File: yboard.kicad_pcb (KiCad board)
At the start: 2 copper layers, 192.5 x 63.5 mm, 27 parts, among them J1 JOYPORT_OUT, J2 CONN_D, J3 CONN_F, SW1 FIRE_BTN, SW2 B_BTN, SW3 A_BTN, SW4 RIGHT_BTN, SW5 LEFT_BTN, SW6 DOWN_BTN, SW7 UP_BTN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

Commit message: YBoard rename within the designs
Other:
- board text added: "YBoard DirBoard v 1.0"
- board text added: "YBoard FireBoard"
- board text removed: "JoyBoard DirBoard v 1.0"
- board text removed: "JoyBoard FireBoard"
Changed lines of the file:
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@@
 	(paper "A4")
 	(title_block
-		(title "Amiga JoyBoard")
+		(title "YBoard")
 		(date "2024-07-12")
-		(rev "1.0")
+		(rev "1.1")
 		(company "Kot_Behemot")
 	)
@@
 		)
 	)
-	(gr_text "JoyBoard FireBoard"
-		(at 190.5 69.85 0)
+	(gr_text "YBoard FireBoard"
+		(at 190.5 70.104 0)
 		(layer "B.Cu" knockout)
 		(effects
@@
 		)
 	)
-	(gr_text "JoyBoard DirBoard\nv 1.0"
+	(gr_text "YBoard DirBoard\nv 1.0"
 		(at 128.524 88.646 0)
 		(layer "B.Cu" knockout)
@@
 	)
 	(gr_text "v 1.0"
-		(at 190.5 73.152 0)
+		(at 190.5762 72.8218 0)
 		(layer "B.Cu" knockout)
 		(effects

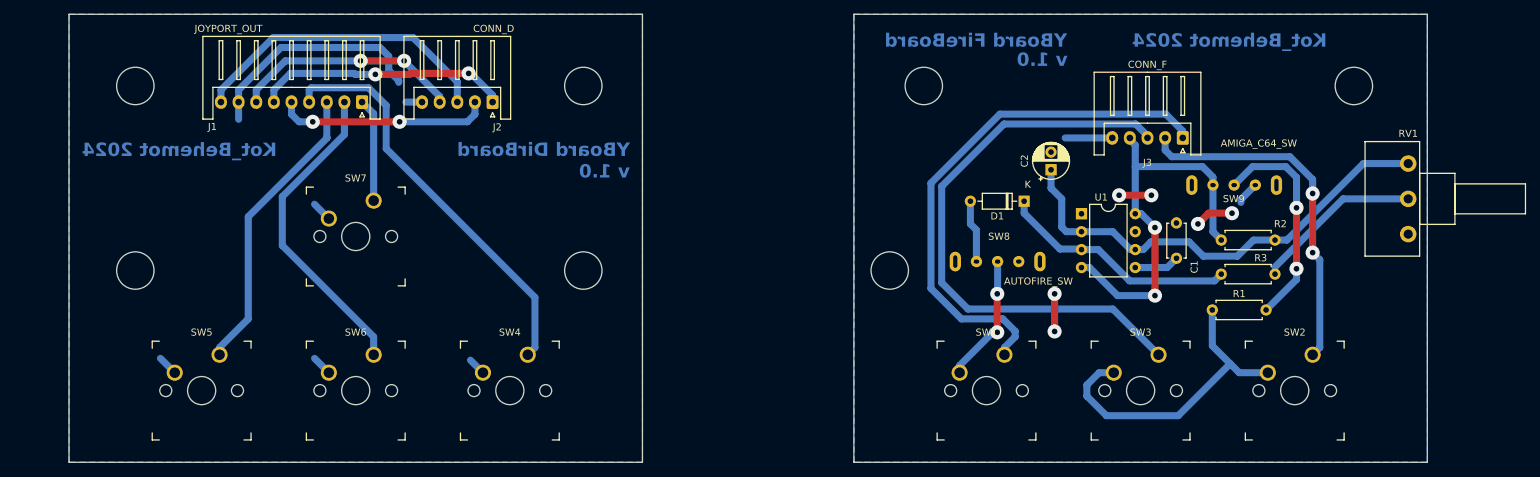
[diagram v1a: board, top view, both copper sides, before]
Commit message: only the board with rounded traces retained
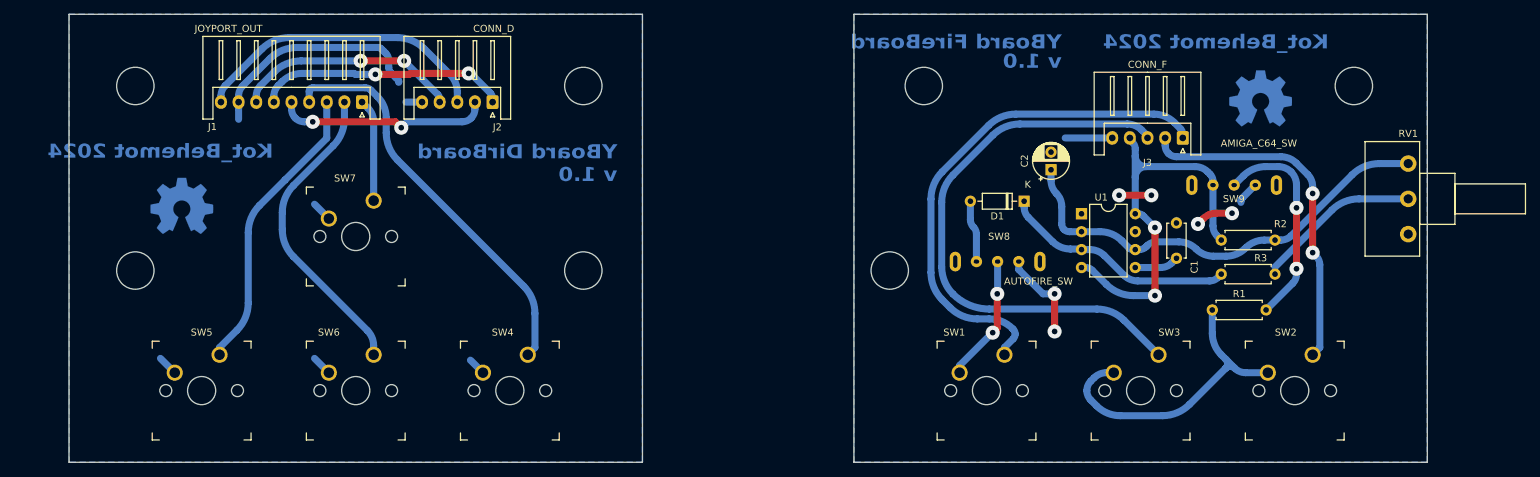
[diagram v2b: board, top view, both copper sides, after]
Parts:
- added REF**: OSHW-Symbol_8.9x8mm_Copper, Symbol:OSHW-Symbol_8.9x8mm_Copper, B.Cu at (217.9, 77.2)
- added REF**: OSHW-Symbol_8.9x8mm_Copper, Symbol:OSHW-Symbol_8.9x8mm_Copper, B.Cu at (65.0, 92.5)
- REF** (x7): footprint MountingHole:MountingHole_5.3mm_M5_DIN965 -> Amiga Joyboard:MountingHole_5.3mm_M5_DIN965_drill_mark
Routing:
- net GND_F: track 25.9 -> 33.4 mm
- net VCC_F: track 57.4 -> 59.6 mm
- net Net-(U1-THR): track 65.9 -> 64.1 mm
- net /FIRE_F: track 75.1 -> 73.4 mm
- net /A_F: track 82.5 -> 80.9 mm
- net /DOWN: track 44.8 -> 43.9 mm
- net /RIGHT: track 58.3 -> 57.5 mm
- net /A_D: track 43.8 -> 43.0 mm
- net Net-(R1-Pad1): track 45.2 -> 45.9 mm
- net /AUTOFIRE: track 34.0 -> 33.4 mm
- net /LEFT: track 42.1 -> 41.6 mm
- net Net-(SW9-B): track 31.1 -> 30.6 mm
- net GND_D: track 46.2 -> 45.6 mm

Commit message: labeling, libraries and other minor fixes
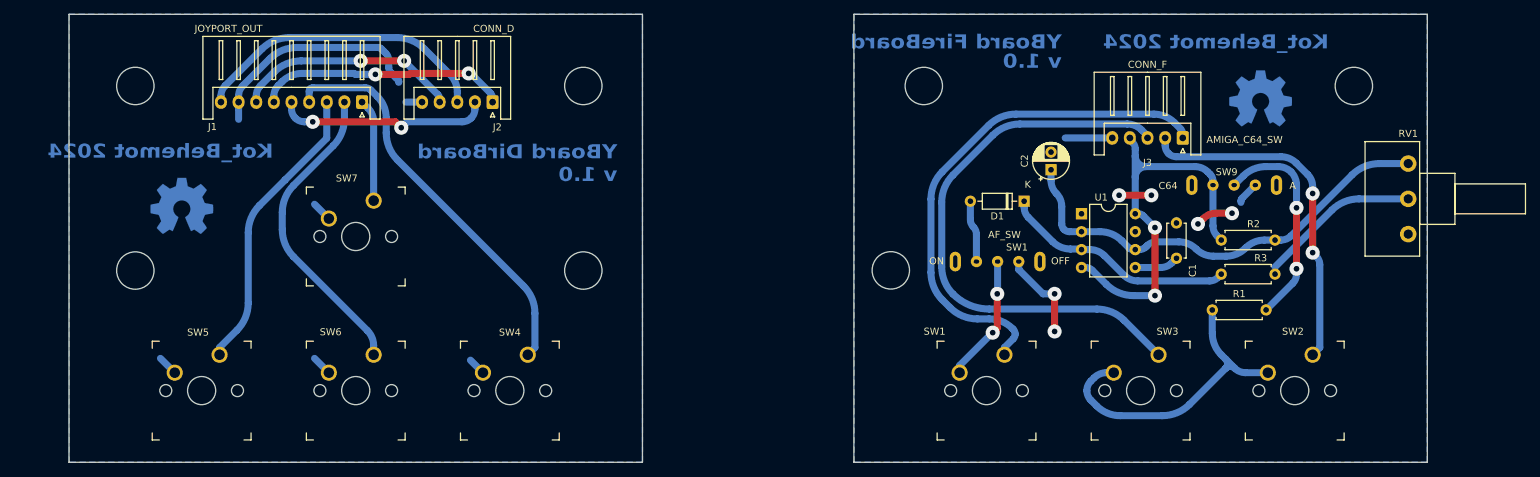
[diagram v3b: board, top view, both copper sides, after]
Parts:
- REF** (x7): footprint Amiga Joyboard:MountingHole_5.3mm_M5_DIN965_drill_mark -> Yboard:MountingHole_5.3mm_M5_DIN965_drill_mark
- SW1, SW2, SW3, SW4, SW5, SW6, SW7: footprint Amiga Joyboard:SW_MX -> Yboard:SW_MX
- SW1: renamed from SW8; value AUTOFIRE_SW -> AF_SW; footprint Amiga Joyboard:SS12T44_SLIDER_SWITCH_SPDT -> Yboard:SS12T44_SLIDER_SWITCH_SPDT
- SW9: footprint Amiga Joyboard:SS12T44_SLIDER_SWITCH_SPDT -> Yboard:SS12T44_SLIDER_SWITCH_SPDT
- moved REF** 0.15 mm to (165.5, 101.6)
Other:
- board text added: "A"
- board text added: "C64"
- board text added: "OFF"
- board text added: "ON"
